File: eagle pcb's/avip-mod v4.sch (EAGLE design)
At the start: 36 parts, among them J4 0ohm, U1 14m2, U2 SN74LVC2G17DBV

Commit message: Updates
Combined non stock items into single lib.
update pcb, clean up some more DRC issues.
reroute some traces to simplify design.
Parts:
- B/PB, CVBS, DA, G/Y, LA, R/PR/C, RA: device adafruit:ANTENNA_U.FL -> XBOX:ANTENNA_U.FL
- JP1, JP2, JP3: value JUMPER-SMT_2_NC_PASTE_NO-SILK -> JUMPER-SMT_NO-SILK; device SparkFun-Jumpers:JUMPER-SMT_2_NC_PASTE_NO-SILK -> XBOX:JUMPER-SMT_NO-SILK
- U1: device picaxe-4:PICAXE-14AXE017M2SM -> XBOX:PICAXE-14AXE017M2SM
- U2: device 74LV:SN74LVC2G17DBV -> XBOX:SN74LVC2G17DBV
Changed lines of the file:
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@@
 <grid distance="0.1" unitdist="inch" unit="inch" style="lines" multiple="1" display="no" altdistance="0.01" altunitdist="inch" altunit="inch"/>
 <layers>
-<layer number="1" name="Top" color="4" fill="1" visible="yes" active="no"/>
-<layer number="16" name="Bottom" color="1" fill="1" visible="yes" active="no"/>
-<layer number="17" name="Pads" color="2" fill="1" visible="yes" active="no"/>
-<layer number="18" name="Vias" color="2" fill="1" visible="yes" active="no"/>
-<layer number="19" name="Unrouted" color="6" fill="1" visible="yes" active="no"/>
-<layer number="20" name="Dimension" color="15" fill="1" visible="yes" active="no"/>
-<layer number="21" name="tPlace" color="7" fill="1" visible="yes" active="no"/>
-<layer number="22" name="bPlace" color="7" fill="1" visible="yes" active="no"/>
-<layer number="23" name="tOrigins" color="15" fill="1" visible="yes" active="no"/>
-<layer number="24" name="bOrigins" color="15" fill="1" visible="yes" active="no"/>
-<layer number="25" name="tNames" color="7" fill="1" visible="yes" active="no"/>
-<layer number="26" name="bNames" color="7" fill="1" visible="yes" active="no"/>
-<layer number="27" name="tValues" color="7" fill="1" visible="yes" active="no"/>
-<layer number="28" name="bValues" color="7" fill="1" visible="yes" active="no"/>
+<layer number="1" name="Top" color="4" fill="1" visible="no" active="no"/>
+<layer number="16" name="Bottom" color="1" fill="1" visible="no" active="no"/>
+<layer number="17" name="Pads" color="2" fill="1" visible="no" active="no"/>
+<layer number="18" name="Vias" color="2" fill="1" visible="no" active="no"/>
+<layer number="19" name="Unrouted" color="6" fill="1" visible="no" active="no"/>
+<layer number="20" name="Dimension" color="15" fill="1" visible="no" active="no"/>
+<layer number="21" name="tPlace" color="7" fill="1" visible="no" active="no"/>
+<layer number="22" name="bPlace" color="7" fill="1" visible="no" active="no"/>
+<layer number="23" name="tOrigins" color="15" fill="1" visible="no" active="no"/>
+<layer number="24" name="bOrigins" color="15" fill="1" visible="no" active="no"/>
+<layer number="25" name="tNames" color="7" fill="1" visible="no" active="no"/>
+<layer number="26" name="bNames" color="7" fill="1" visible="no" active="no"/>
+<layer number="27" name="tValues" color="7" fill="1" visible="no" active="no"/>
+<layer number="28" name="bValues" color="7" fill="1" visible="no" active="no"/>
 <layer number="29" name="tStop" color="7" fill="3" visible="no" active="no"/>
 <layer number="30" name="bStop" color="7" fill="6" visible="no" active="no"/>
@@
 <layer number="35" name="tGlue" color="7" fill="4" visible="no" active="no"/>
 <layer number="36" name="bGlue" color="7" fill="5" visible="no" active="no"/>
-<layer number="37" name="tTest" color="7" fill="1" visible="yes" active="no"/>
-<layer number="38" name="bTest" color="7" fill="1" visible="yes" active="no"/>
+<layer number="37" name="tTest" color="7" fill="1" visible="no" active="no"/>
+<layer number="38" name="bTest" color="7" fill="1" visible="no" active="no"/>
 <layer number="39" name="tKeepout" color="4" fill="11" visible="no" active="no"/>
 <layer number="40" name="bKeepout" color="1" fill="11" visible="no" active="no"/>
@@
 <layer number="44" name="Drills" color="7" fill="1" visible="no" active="no"/>
 <layer number="45" name="Holes" color="7" fill="1" visible="no" active="no"/>
-<layer number="46" name="Milling" color="3" fill="1" visible="yes" active="no"/>
-<layer number="47" name="Measures" color="7" fill="1" visible="yes" active="no"/>
-<layer number="48" name="Document" color="7" fill="1" visible="yes" active="no"/>
-<layer number="49" name="Reference" color="7" fill="1" visible="yes" active="no"/>
-<layer number="50" name="dxf" color="7" fill="1" visible="yes" active="no"/>
-<layer number="51" name="tDocu" color="7" fill="1" visible="yes" active="no"/>
-<layer number="52" name="bDocu" color="7" fill="1" visible="yes" active="no"/>
-<layer number="53" name="tGND_GNDA" color="7" fill="9" visible="yes" active="no"/>
-<layer number="54" name="bGND_GNDA" color="1" fill="9" visible="yes" active="no"/>
-<layer number="56" name="wert" color="7" fill="1" visible="yes" active="no"/>
-<layer number="57" name="tCAD" color="7" fill="1" visible="yes" active="no"/>
-<layer number="59" name="tCarbon" color="7" fill="1" visible="yes" active="no"/>
-<layer number="60" name="bCarbon" color="7" fill="1" visible="yes" active="no"/>
+<layer number="46" name="Milling" color="3" fill="1" visible="no" active="no"/>
+<layer number="47" name="Measures" color="7" fill="1" visible="no" active="no"/>
+<layer number="48" name="Document" color="7" fill="1" visible="no" active="no"/>
+<layer number="49" name="Reference" color="7" fill="1" visible="no" active="no"/>
+<layer number="50" name="dxf" color="7" fill="1" visible="no" active="no"/>
+<layer number="51" name="tDocu" color="7" fill="1" visible="no" active="no"/>
+<layer number="52" name="bDocu" color="7" fill="1" visible="no" active="no"/>
+<layer number="53" name="tGND_GNDA" color="7" fill="9" visible="no" active="no"/>
+<layer number="54" name="bGND_GNDA" color="1" fill="9" visible="no" active="no"/>
+<layer number="56" name="wert" color="7" fill="1" visible="no" active="no"/>
+<layer number="57" name="tCAD" color="7" fill="1" visible="no" active="no"/>
+<layer number="59" name="tCarbon" color="7" fill="1" visible="no" active="no"/>
+<layer number="60" name="bCarbon" color="7" fill="1" visible="no" active="no"/>
 <layer number="88" name="SimResults" color="9" fill="1" visible="yes" active="yes"/>
 <layer number="89" name="SimProbes" color="9" fill="1" visible="yes" active="yes"/>
@@
 </classes>
 <parts>
-<part name="U1" library="picaxe-4" deviceset="PICAXE-14" device="AXE017M2SM" value="14m2"/>
-<part name="B/PB" library="adafruit" deviceset="ANTENNA_U.FL" device="" value="75 ohm"/>
-<part name="R/PR/C" library="adafruit" deviceset="ANTENNA_U.FL" device="" value="75 ohm"/>
-<part name="G/Y" library="adafruit" deviceset="ANTENNA_U.FL" device="" value="75 ohm"/>
+<part name="U1" library="XBOX" deviceset="PICAXE-14" device="AXE017M2SM" value="14m2"/>
+<part name="B/PB" library="XBOX" deviceset="ANTENNA_U.FL" device="" value="75 ohm"/>
+<part name="R/PR/C" library="XBOX" deviceset="ANTENNA_U.FL" device="" value="75 ohm"/>
+<part name="G/Y" library="XBOX" deviceset="ANTENNA_U.FL" device="" value="75 ohm"/>
 <part name="AVIP" library="XBOX" deviceset="AVIP" device="1.0-1.5"/>
-<part name="CVBS" library="adafruit" deviceset="ANTENNA_U.FL" device="" value="75 ohm"/>
-<part name="RA" library="adafruit" deviceset="ANTENNA_U.FL" device="" value="50-75 ohm"/>
-<part name="LA" library="adafruit" deviceset="ANTENNA_U.FL" device="" value="50-75 ohm"/>
-<part name="DA" library="adafruit" deviceset="ANTENNA_U.FL" device="" value="75 ohm"/>
+<part name="CVBS" library="XBOX" deviceset="ANTENNA_U.FL" device="" value="75 ohm"/>
+<part name="RA" library="XBOX" deviceset="ANTENNA_U.FL" device="" value="50-75 ohm"/>
+<part name="LA" library="XBOX" deviceset="ANTENNA_U.FL" device="" value="50-75 ohm"/>
+<part name="DA" library="XBOX" deviceset="ANTENNA_U.FL" device="" value="75 ohm"/>
 <part name="P+1" library="supply1" library_urn="urn:adsk.eagle:library:371" deviceset="VCC" device=""/>
 <part name="SUPPLY2" library="supply2" library_urn="urn:adsk.eagle:library:372" deviceset="GND" device=""/>
@@
 <part name="C2" library="rcl" library_urn="urn:adsk.eagle:library:334" deviceset="C-EU" device="C0603" package3d_urn="urn:adsk.eagle:package:23616/2" value="100nf"/>
 <part name="SUPPLY1" library="supply2" library_urn="urn:adsk.eagle:library:372" deviceset="GND" device=""/>
-<part name="U2" library="74LV" deviceset="SN74LVC2G17" device="DBV"/>
+<part name="U2" library="XBOX" deviceset="SN74LVC2G17" device="DBV"/>
 <part name="C3" library="rcl" library_urn="urn:adsk.eagle:library:334" deviceset="C-EU" device="C0603" package3d_urn="urn:adsk.eagle:package:23616/2" value="100nf"/>
-<part name="JP1" library="SparkFun-Jumpers" deviceset="JUMPER-SMT_2_NC_PASTE" device="_NO-SILK" package3d_urn="urn:adsk.eagle:package:39283/1"/>
-<part name="JP2" library="SparkFun-Jumpers" deviceset="JUMPER-SMT_2_NC_PASTE" device="_NO-SILK" package3d_urn="urn:adsk.eagle:package:39283/1"/>
-<part name="JP3" library="SparkFun-Jumpers" deviceset="JUMPER-SMT_2_NC_PASTE" device="_NO-SILK" package3d_urn="urn:adsk.eagle:package:39283/1"/>
+<part name="JP1" library="XBOX" deviceset="JUMPER-SMT" device="_NO-SILK" package3d_urn="urn:adsk.eagle:package:39283/1"/>
+<part name="JP2" library="XBOX" deviceset="JUMPER-SMT" device="_NO-SILK" package3d_urn="urn:adsk.eagle:package:39283/1"/>
+<part name="JP3" library="XBOX" deviceset="JUMPER-SMT" device="_NO-SILK" package3d_urn="urn:adsk.eagle:package:39283/1"/>
 </parts>
 <sheets>

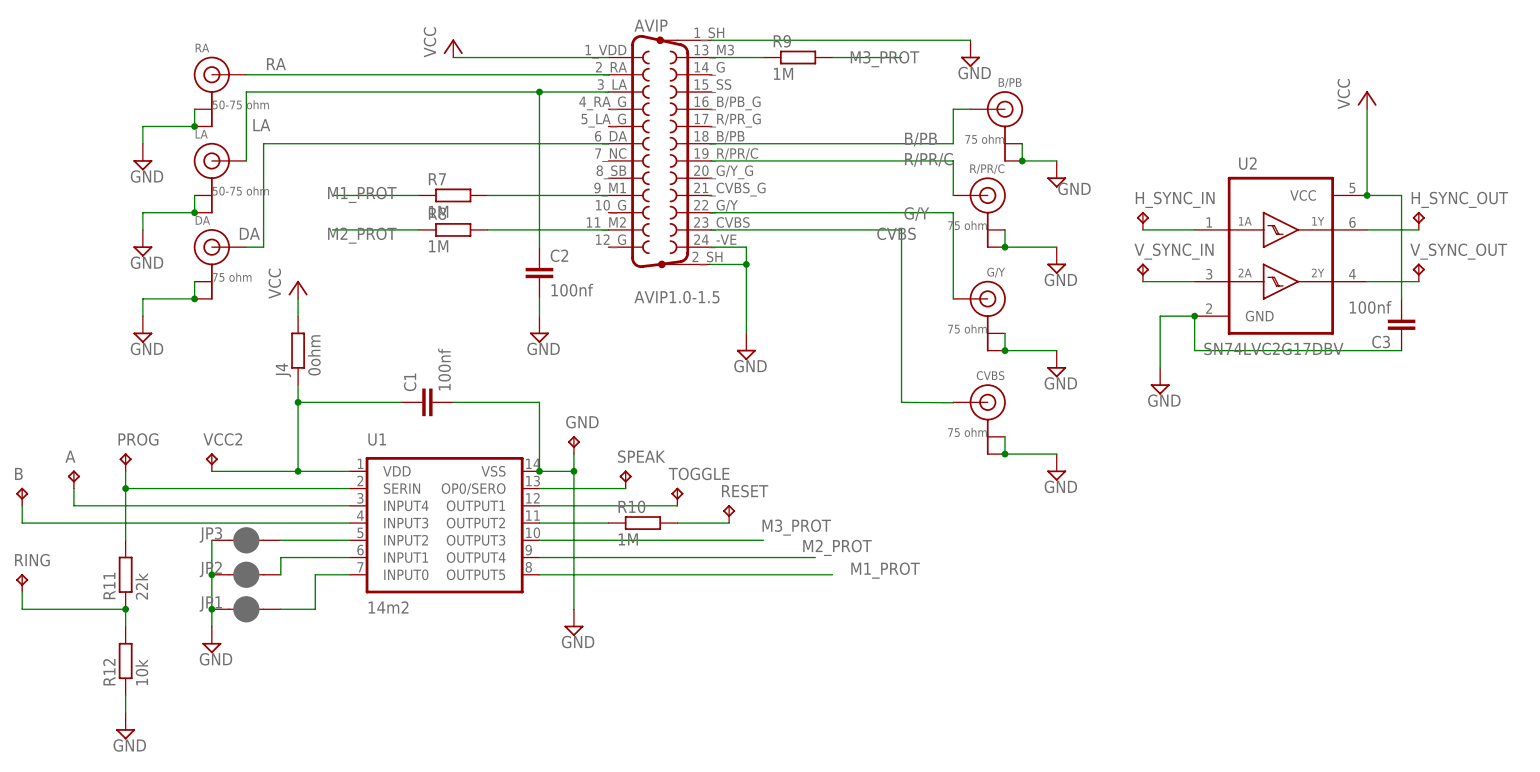
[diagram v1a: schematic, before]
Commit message: Fix PCB preview and update pictures
Conflict between mill and dimensions layer causing all PCB's to not show up in manufacture preview.
Add pictures of v3, v4 and v4 top PCB.
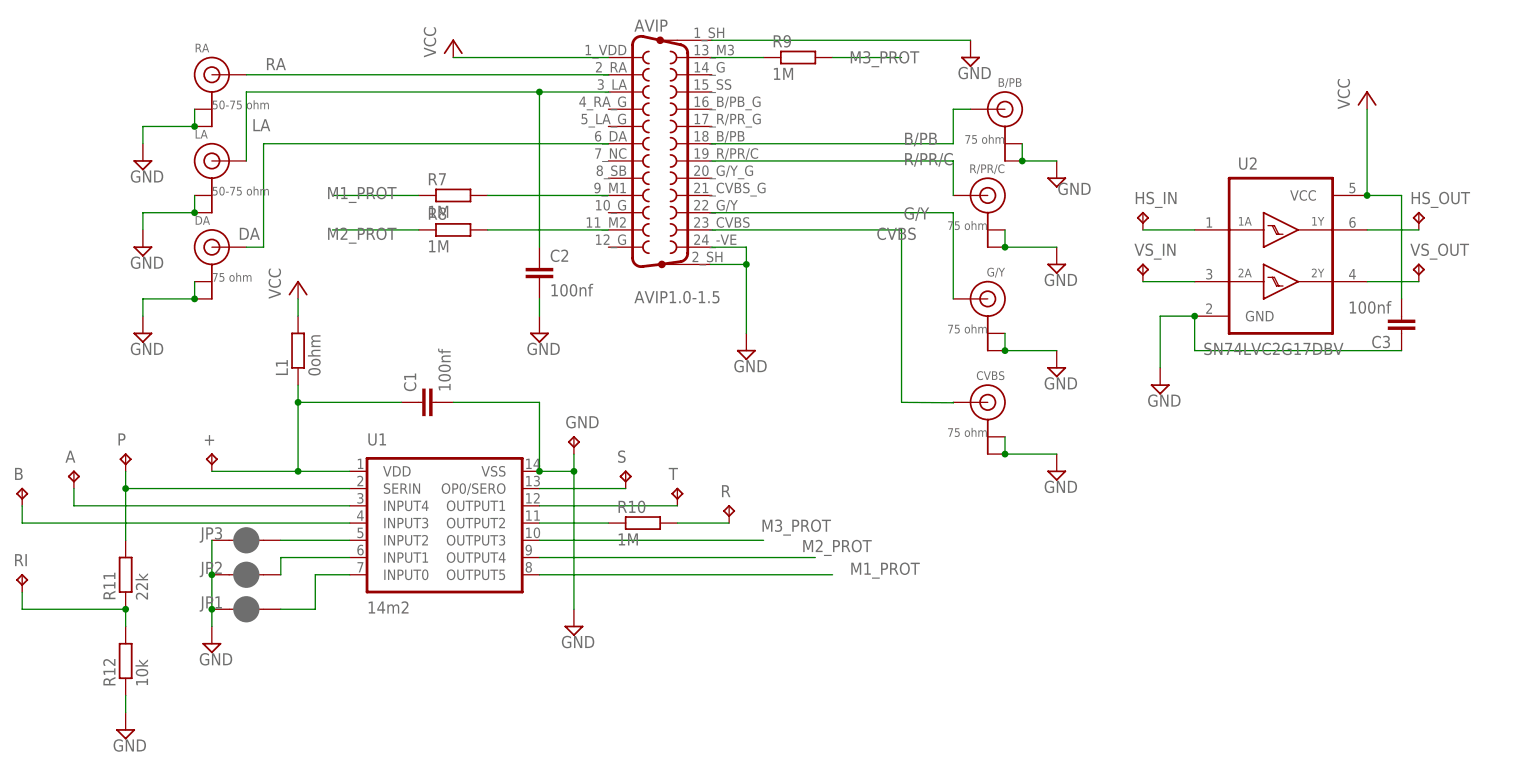
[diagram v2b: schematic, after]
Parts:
- renumbered H_SYNC_IN to HS_IN, H_SYNC_OUT to HS_OUT, J4 to L1, PROG to P, RESET to R, RING to RI, SPEAK to S, TOGGLE to T, VCC2 to +, V_SYNC_IN to VS_IN, V_SYNC_OUT to VS_OUT
